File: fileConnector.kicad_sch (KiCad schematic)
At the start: 9 parts

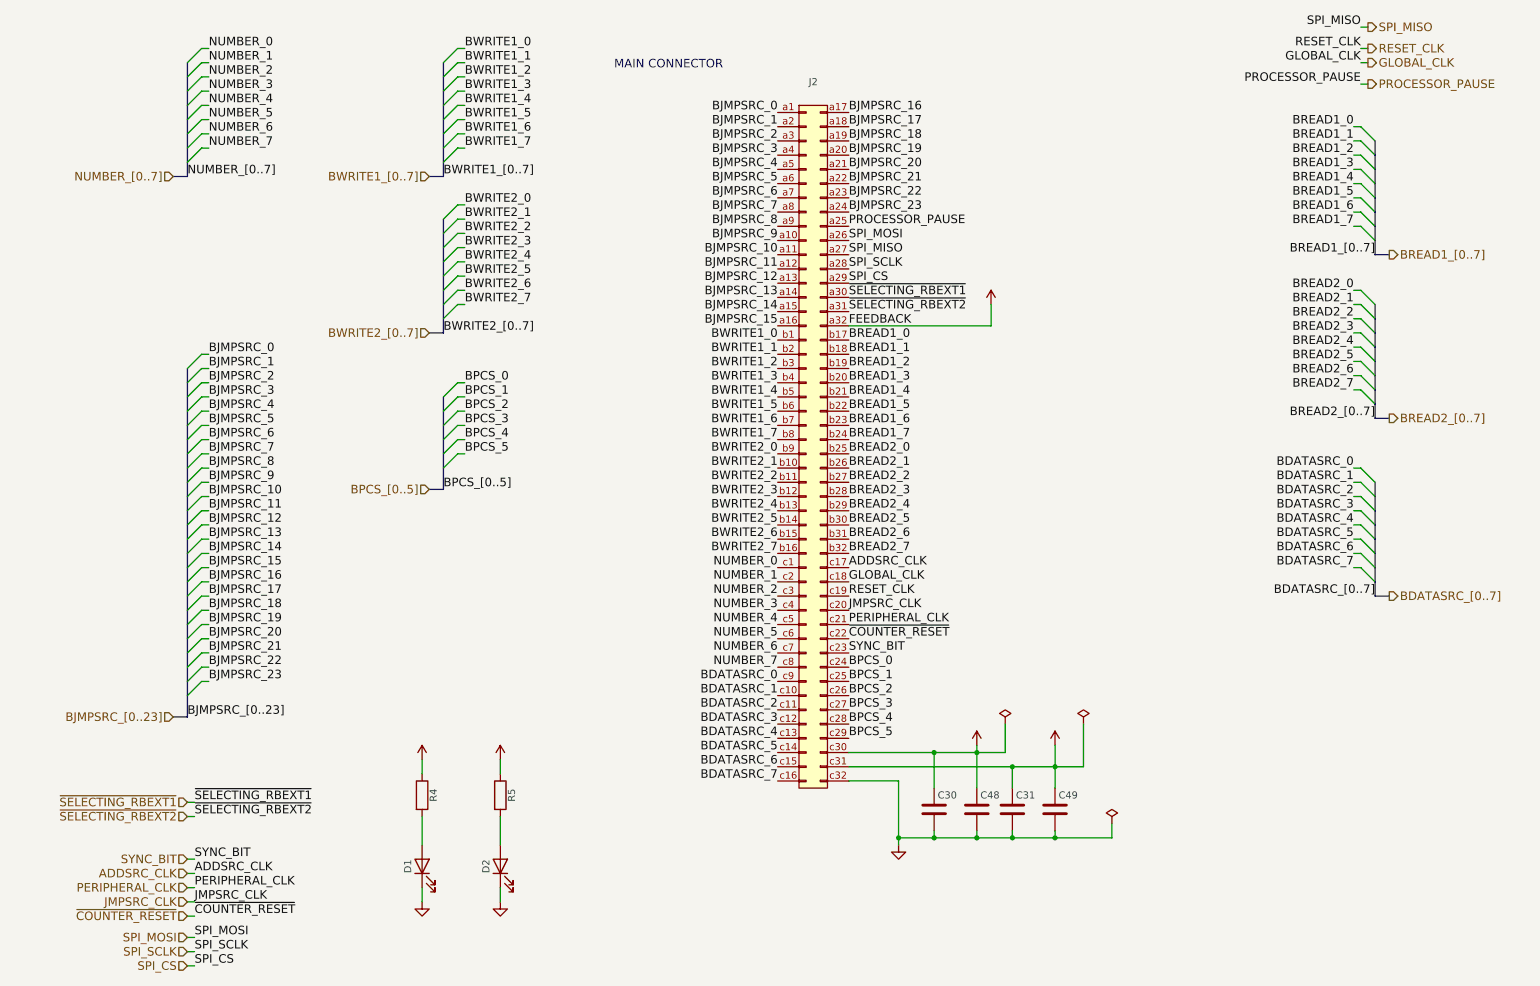
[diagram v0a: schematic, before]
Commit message: Updating descriptions
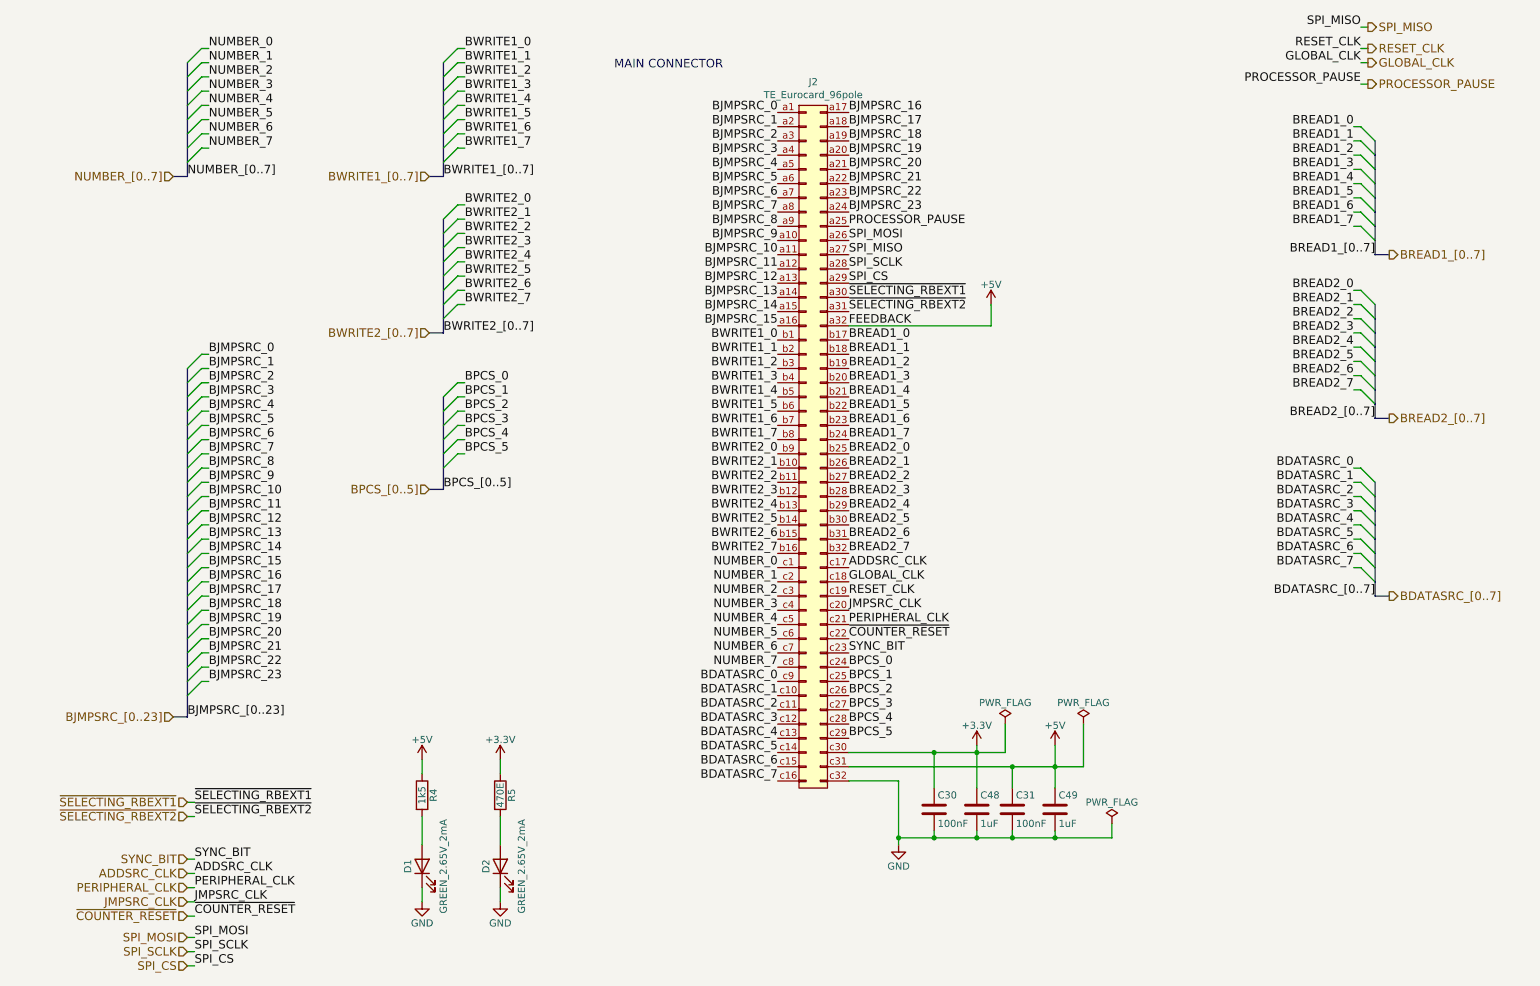
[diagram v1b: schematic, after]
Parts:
- C30, C31: value (none) -> 100nF; footprint (none) -> Capacitor_SMD:C_0805_2012Metric
- C48, C49: value (none) -> 1uF; footprint (none) -> Capacitor_SMD:C_0805_2012Metric
- D1, D2: value (none) -> GREEN_2.65V_2mA; footprint (none) -> LED_SMD:LED_1206_3216Metric
- J2: value (none) -> TE_Eurocard_96pole; footprint (none) -> Eurocard_5536475-1:Eurocard_5536475-1
- R4: value (none) -> 1k5; footprint (none) -> Resistor_SMD:R_0805_2012Metric
- R5: value (none) -> 470E; footprint (none) -> Resistor_SMD:R_0805_2012Metric
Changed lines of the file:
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@@
   (title_block
     (title "GP8B")
-    (date "2021-03-04")
-    (rev "V5.1")
+    (date "2022-07-08")
+    (rev "V6.0")
     (company "Guillaume Guillet")
-    (comment 1 "Copyright Guillaume Guillet 2021")
+    (comment 1 "Copyright Guillaume Guillet 2022")
     (comment 2 "Licensed under CERN-OHL-W v2 or later")
   )
@@
       (effects (font (size 1.27 1.27)) hide)
     )
-    (property "Value" "" (id 1) (at 198.12 138.43 0))
+    (property "Value" "PWR_FLAG" (id 1) (at 198.12 138.43 0))
     (property "Footprint" "" (id 2) (at 198.12 142.24 0)
       (effects (font (size 1.27 1.27)) hide)
@@
       (effects (font (size 1.27 1.27)) hide)
     )
-    (property "Value" "" (id 1) (at 184.15 138.43 0))
+    (property "Value" "PWR_FLAG" (id 1) (at 184.15 138.43 0))
     (property "Footprint" "" (id 2) (at 184.15 142.24 0)
       (effects (font (size 1.27 1.27)) hide)
@@
       (effects (font (size 1.27 1.27)) hide)
     )
-    (property "Value" "" (id 1) (at 203.2 156.21 0))
+    (property "Value" "PWR_FLAG" (id 1) (at 203.2 156.21 0))
     (property "Footprint" "" (id 2) (at 203.2 160.02 0)
       (effects (font (size 1.27 1.27)) hide)
@@
       (effects (font (size 1.27 1.27)) hide)
     )
-    (property "Value" "" (id 1) (at 179.07 142.494 0))
+    (property "Value" "+3.3V" (id 1) (at 179.07 142.494 0))
     (property "Footprint" "" (id 2) (at 179.07 146.05 0)
       (effects (font (size 1.27 1.27)) hide)
@@
       (effects (font (size 1.27 1.27)) (justify left))
     )
-    (property "Value" "" (id 1) (at 172.085 160.02 0)
+    (property "Value" "100nF" (id 1) (at 172.085 160.02 0)
       (effects (font (size 1.27 1.27)) (justify left))
     )
-    (property "Footprint" "" (id 2) (at 172.4152 161.29 0)
+    (property "Footprint" "Capacitor_SMD:C_0805_2012Metric" (id 2) (at 172.4152 161.29 0)
       (effects (font (size 1.27 1.27)) hide)
     )
@@
       (effects (font (size 1.27 1.27)) (justify left))
     )
-    (property "Value" "" (id 1) (at 186.055 160.02 0)
+    (property "Value" "100nF" (id 1) (at 186.055 160.02 0)
       (effects (font (size 1.27 1.27)) (justify left))
     )
-    (property "Footprint" "" (id 2) (at 186.3852 161.29 0)
+    (property "Footprint" "Capacitor_SMD:C_0805_2012Metric" (id 2) (at 186.3852 161.29 0)
       (effects (font (size 1.27 1.27)) hide)
     )
@@
       (effects (font (size 1.27 1.27)) hide)
     )
-    (property "Value" "" (id 1) (at 165.1 167.64 0))
+    (property "Value" "GND" (id 1) (at 165.1 167.64 0))
     (property "Footprint" "" (id 2) (at 165.1 163.83 0)
       (effects (font (size 1.27 1.27)) hide)
@@
       (effects (font (size 1.27 1.27)) hide)
     )
-    (property "Value" "" (id 1) (at 193.04 142.494 0))
+    (property "Value" "+5V" (id 1) (at 193.04 142.494 0))
     (property "Footprint" "" (id 2) (at 193.04 146.05 0)
       (effects (font (size 1.27 1.27)) hide)
@@
     (in_bom yes) (on_board yes)
     (property "Reference" "R4" (id 0) (at 82.042 154.94 90))
-    (property "Value" "" (id 1) (at 80.01 154.94 90))
-    (property "Footprint" "" (id 2) (at 78.232 154.94 90)
+    (property "Value" "1k5" (id 1) (at 80.01 154.94 90))
+    (property "Footprint" "Resistor_SMD:R_0805_2012Metric" (id 2) (at 78.232 154.94 90)
       (effects (font (size 1.27 1.27)) hide)
     )
@@
     (in_bom yes) (on_board yes)
     (property "Reference" "D1" (id 0) (at 77.47 167.64 0))
-    (property "Value" "" (id 1) (at 83.82 167.64 0))
-    (property "Footprint" "" (id 2) (at 80.01 167.64 0)
+    (property "Value" "GREEN_2.65V_2mA" (id 1) (at 83.82 167.64 0))
+    (property "Footprint" "LED_SMD:LED_1206_3216Metric" (id 2) (at 80.01 167.64 0)
       (effects (font (size 1.27 1.27)) hide)
     )
@@
       (effects (font (size 1.27 1.27)) hide)
     )
-    (property "Value" "" (id 1) (at 80.01 145.034 0))
+    (property "Value" "+5V" (id 1) (at 80.01 145.034 0))
     (property "Footprint" "" (id 2) (at 80.01 148.59 0)
       (effects (font (size 1.27 1.27)) hide)
@@
       (effects (font (size 1.27 1.27)) hide)
     )
-    (property "Value" "" (id 1) (at 80.01 177.8 0))
+    (property "Value" "GND" (id 1) (at 80.01 177.8 0))
     (property "Footprint" "" (id 2) (at 80.01 173.99 0)
       (effects (font (size 1.27 1.27)) hide)
@@
       (effects (font (size 1.27 1.27)) hide)
     )
-    (property "Value" "" (id 1) (at 93.98 145.034 0))
+    (property "Value" "+3.3V" (id 1) (at 93.98 145.034 0))
     (property "Footprint" "" (id 2) (at 93.98 148.59 0)
       (effects (font (size 1.27 1.27)) hide)
@@
     (in_bom yes) (on_board yes)
     (property "Reference" "R5" (id 0) (at 96.012 154.94 90))
-    (property "Value" "" (id 1) (at 93.98 154.94 90))
-    (property "Footprint" "" (id 2) (at 92.202 154.94 90)
+    (property "Value" "470E" (id 1) (at 93.98 154.94 90))
+    (property "Footprint" "Resistor_SMD:R_0805_2012Metric" (id 2) (at 92.202 154.94 90)
       (effects (font (size 1.27 1.27)) hide)
     )
@@
       (effects (font (size 1.27 1.27)) hide)
     )
-    (property "Value" "" (id 1) (at 93.98 177.8 0))
+    (property "Value" "GND" (id 1) (at 93.98 177.8 0))
     (property "Footprint" "" (id 2) (at 93.98 173.99 0)
       (effects (font (size 1.27 1.27)) hide)
@@
     (in_bom yes) (on_board yes)
     (property "Reference" "D2" (id 0) (at 91.44 167.64 0))
-    (property "Value" "" (id 1) (at 97.79 167.64 0))
-    (property "Footprint" "" (id 2) (at 93.98 167.64 0)
+    (property "Value" "GREEN_2.65V_2mA" (id 1) (at 97.79 167.64 0))
+    (property "Footprint" "LED_SMD:LED_1206_3216Metric" (id 2) (at 93.98 167.64 0)
       (effects (font (size 1.27 1.27)) hide)
     )
@@
     (in_bom yes) (on_board yes)
     (property "Reference" "J2" (id 0) (at 149.86 27.559 0))
-    (property "Value" "" (id 1) (at 149.86 29.8704 0))
-    (property "Footprint" "" (id 2) (at 148.59 81.28 0)
+    (property "Value" "TE_Eurocard_96pole" (id 1) (at 149.86 29.8704 0))
+    (property "Footprint" "Eurocard_5536475-1:Eurocard_5536475-1" (id 2) (at 148.59 81.28 0)
       (effects (font (size 1.27 1.27)) hide)
     )
@@
       (effects (font (size 1.27 1.27)) hide)
     )
-    (property "Value" "" (id 1) (at 181.61 63.754 0))
+    (property "Value" "+5V" (id 1) (at 181.61 63.754 0))
     (property "Footprint" "" (id 2) (at 181.61 67.31 0)
       (effects (font (size 1.27 1.27)) hide)
@@
       (effects (font (size 1.27 1.27)) (justify left))
     )
-    (property "Value" "" (id 1) (at 179.705 160.02 0)
+    (property "Value" "1uF" (id 1) (at 179.705 160.02 0)
       (effects (font (size 1.27 1.27)) (justify left))
     )
-    (property "Footprint" "" (id 2) (at 180.0352 161.29 0)
+    (property "Footprint" "Capacitor_SMD:C_0805_2012Metric" (id 2) (at 180.0352 161.29 0)
       (effects (font (size 1.27 1.27)) hide)
     )
@@
       (effects (font (size 1.27 1.27)) (justify left))
     )
-    (property "Value" "" (id 1) (at 193.675 160.02 0)
+    (property "Value" "1uF" (id 1) (at 193.675 160.02 0)
       (effects (font (size 1.27 1.27)) (justify left))
     )
-    (property "Footprint" "" (id 2) (at 194.0052 161.29 0)
-      (effects (font (size 1.27 1.27)) hide)
-    )
+    (property "Footprint" "Capacitor_SMD:C_0805_2012Metric" (id 2) (at 194.0052 161.29 0)
+      (effects (font (size 1.27 1.27)) hide)
+    )

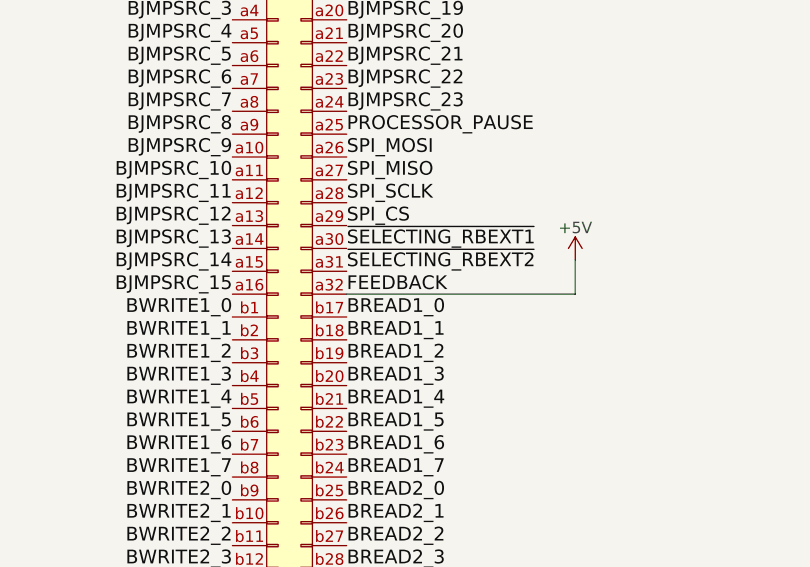
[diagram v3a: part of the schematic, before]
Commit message: Finally remove clock sync, big improvement for the "if" instruction check (faster tps, less gates)
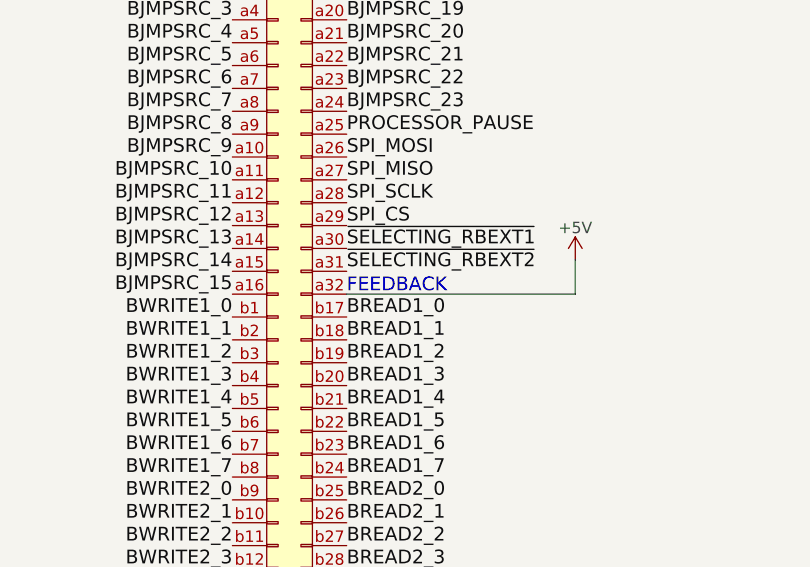
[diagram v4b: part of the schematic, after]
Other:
- note added: "FEEDBACK"
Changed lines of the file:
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@@
+    (effects (font (size 1.524 1.524)) (justify left bottom))
+  )
+  (text "FEEDBACK" (at 156.21 71.12 0)
     (effects (font (size 1.524 1.524)) (justify left bottom))
   )
@@
     (effects (font (size 1.524 1.524)) (justify left bottom))
   )
-  (label "FEEDBACK" (at 156.21 71.12 0)
-    (effects (font (size 1.524 1.524)) (justify left bottom))
-  )
